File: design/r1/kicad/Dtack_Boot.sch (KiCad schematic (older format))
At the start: 7 parts, among them IC5 ATF16V8QL-15PU, IC6 74174N

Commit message: Initial cleanup
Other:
- note added: "1"
- note added: "Copyright ©2019-2020 Ross Bamford and Contributors.\nOpen Source Hardware licenced under CERN Open Hardware Licence. \nSee https://github.com/roscopeco/rosco_m68k/blob/master/LICENCE.hardware.txt\nOSHWA UK000006 (https://certification.oshwa.org/uk000006.html)\n"
- note added: "DTACK & BOOT"
- note removed: "DTACK\n& BOOT"
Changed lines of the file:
@@
 	6600 2000 6700 1900
-$Comp
-L rosco_m68k-eagle-import:A3L-LOC #FRAME3
-U 1 1 578F4FA5
-P 250 9450
-AR Path="/578F4FA5" Ref="#FRAME3"  Part="1"
-AR Path="/5E53B810/578F4FA5" Ref="#FRAME3"  Part="1"
-F 0 "#FRAME3" H 250 9450 50  0001 C CNN
-F 1 "BOOT line generator" H 250 9450 50  0001 C CNN
-F 2 "" H 250 9450 50  0001 C CNN
-F 3 "" H 250 9450 50  0001 C CNN
-	1    250  9450
-	1    0    0    -1
-$EndComp
 $Comp
 L rosco_m68k-eagle-import:74174N IC6
@@
 Text Notes 5500 7700 0    59   ~ 0
 /BOOT LINE GENERATOR
-Text Notes 13000 10200 0    170  ~ 0
-DTACK\n& BOOT
 NoConn ~ 5300 2900
 NoConn ~ 6200 6200
 NoConn ~ 6200 6500
 NoConn ~ 5300 2200
+Text Notes 12300 10000 0    59   ~ 0
+Copyright ©2019-2020 Ross Bamford and Contributors.\nOpen Source Hardware licenced under CERN Open Hardware Licence. \nSee https://github.com/roscopeco/rosco_m68k/blob/master/LICENCE.hardware.txt\nOSHWA UK000006 (https://certification.oshwa.org/uk000006.html)\n
+Text Notes 12650 10550 0    59   ~ 0
+DTACK & BOOT
+Text Notes 15900 10700 0    59   ~ 0
+1
 Wire Bus Line
 	6700 800  6700 2600

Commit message: Cleanup first pass
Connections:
- net labels added: BOOT, IACK, IODTACK, MFPDS, RAMOE, RW
- net labels removed: /BOOT, /IACK, /IODTACK, /MFPDS, /RAMOE, CONTROL:AS,BERR,BG,BGACK,BR,CLK,DTACK,EVENRAMSEL,EVENROMSEL,EXPSEL,FC0,FC1,FC2,IOSEL,IPL0,IPL1,IPL2,LDS,ODDRAMSEL,ODDROMSEL,RESET,R/W,UDS, R/W
- wire segments 77 -> 65
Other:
- moved on the sheet: IC6A

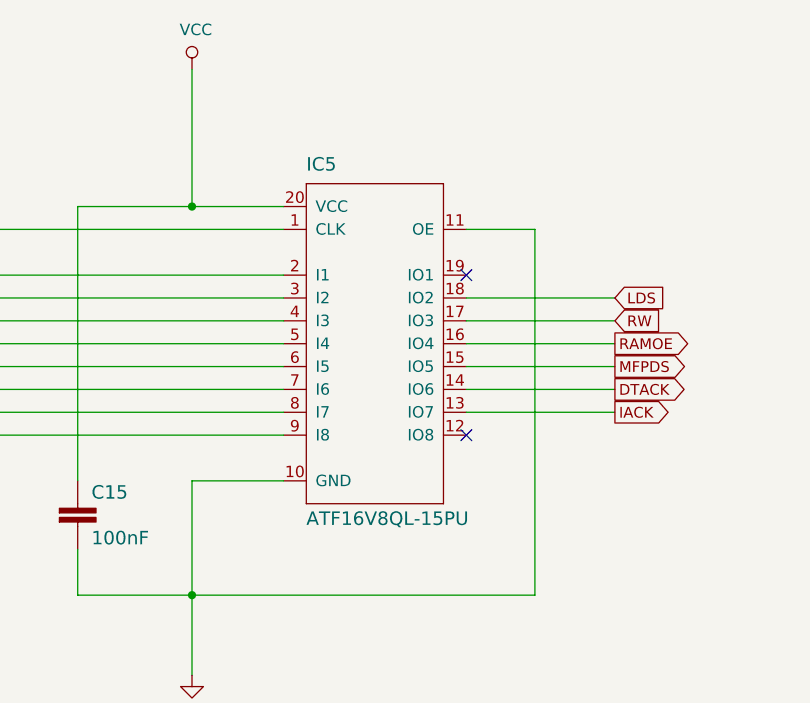
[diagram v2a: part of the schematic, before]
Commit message: Fixing migrated symbols
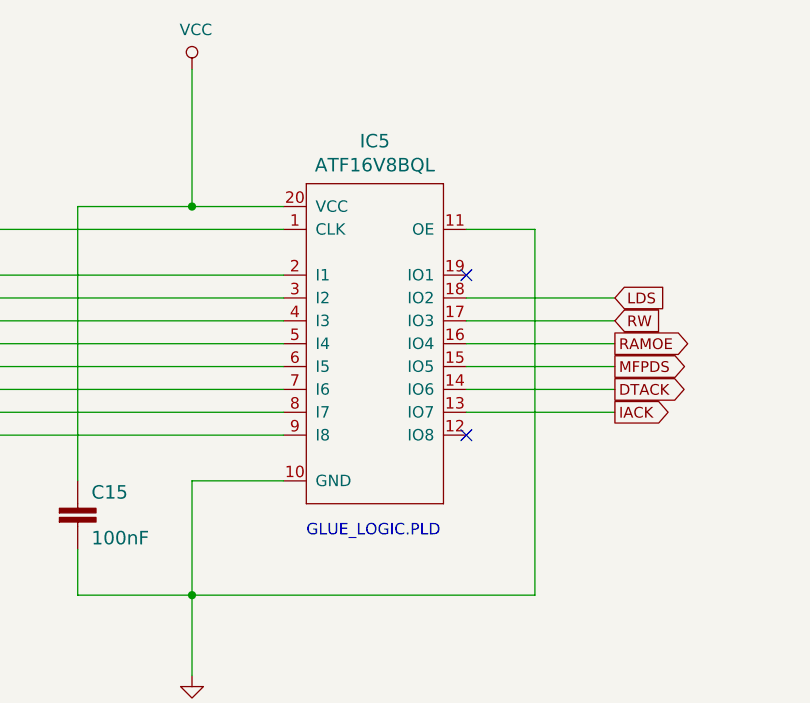
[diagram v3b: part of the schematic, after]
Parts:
- IC5: value ATF16V8QL-15PU -> ATF16V8BQL; footprint rosco_m68k:DIL20 -> (none); MPN ATF16V8QL-15PU -> (none); PROG GLUE_LOGIC.PLD -> (none)
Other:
- note added: "GLUE_LOGIC.PLD"
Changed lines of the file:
@@
-$EndComp
-$Comp
-L rosco_m68k-eagle-import:ATF16V8BP3 IC5
-U 1 1 608347BB
-P 4900 2500
-AR Path="/608347BB" Ref="IC5"  Part="1"
-AR Path="/5E53B810/608347BB" Ref="IC5"  Part="1"
-F 0 "IC5" H 4600 3250 59  0000 L BNN
-F 1 "ATF16V8QL-15PU" H 4600 1700 59  0000 L BNN
-F 2 "rosco_m68k:DIL20" H 4900 2500 50  0001 C CNN
-F 3 "" H 4900 2500 50  0001 C CNN
-F 4 "ATF16V8QL-15PU" H 4900 2500 59  0001 L BNN "MPN"
-F 5 "GLUE_LOGIC.PLD" H 4600 1600 59  0001 L BNN "PROG"
-	1    4900 2500
-	1    0    0    -1
 $EndComp
 $Comp
@@
 Wire Wire Line
 	13200 3150 13200 4200
+$Comp
+L rosco_m68k-eagle-import:ATF16V8BP3 IC5
+U 1 1 5FE89F94
+P 4900 2500
+F 0 "IC5" H 4900 3386 59  0000 C CNN
+F 1 "ATF16V8BQL" H 4900 3281 59  0000 C CNN
+F 2 "" H 4900 2500 50  0001 C CNN
+F 3 "" H 4900 2500 50  0001 C CNN
+	1    4900 2500
+	1    0    0    -1
+$EndComp
+Text Notes 4600 3350 0    50   ~ 0
+GLUE_LOGIC.PLD
 $EndSCHEMATC

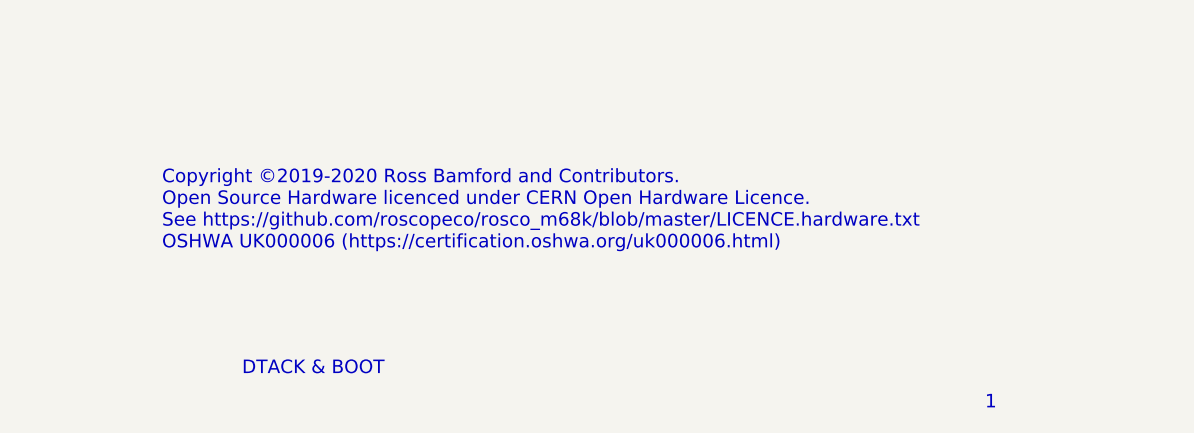
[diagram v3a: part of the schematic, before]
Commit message: Fix #18 and apply suggestions from #17
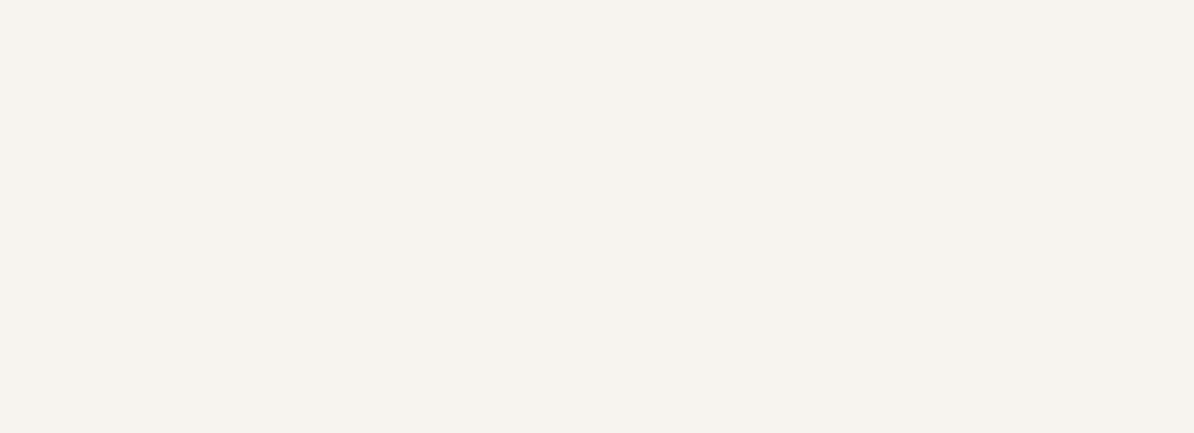
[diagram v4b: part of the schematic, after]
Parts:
- IC5: footprint (none) -> rosco_m68k:DIL20
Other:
- note removed: "1"
- note removed: "Copyright ©2019-2020 Ross Bamford and Contributors.\nOpen Source Hardware licenced under CERN Open Hardware Licence. \nSee https://github.com/roscopeco/rosco_m68k/blob/master/LICENCE.hardware.txt\nOSHWA UK000006 (https://certification.oshwa.org/uk000006.html)\n"
- note removed: "DTACK & BOOT"
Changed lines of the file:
@@
 encoding utf-8
 Sheet 4 6
-Title ""
+Title "DTACK & BOOT"
 Date "2020-02-25"
-Rev ""
+Rev "1"
 Comp ""
-Comment1 ""
-Comment2 ""
-Comment3 ""
-Comment4 ""
+Comment1 "OSHWA UK000006 (https://certification.oshwa.org/uk000006.html)"
+Comment2 "See https://github.com/roscopeco/rosco_m68k/blob/master/LICENCE.hardware.txt"
+Comment3 "Open Source Hardware licenced under CERN Open Hardware Licence"
+Comment4 "Copyright 2019-2020 Ross Bamford and Contributors"
 $EndDescr
 Wire Wire Line
@@
 NoConn ~ 5200 7750
 NoConn ~ 5300 2200
-Text Notes 12300 10000 0    59   ~ 0
-Copyright ©2019-2020 Ross Bamford and Contributors.\nOpen Source Hardware licenced under CERN Open Hardware Licence. \nSee https://github.com/roscopeco/rosco_m68k/blob/master/LICENCE.hardware.txt\nOSHWA UK000006 (https://certification.oshwa.org/uk000006.html)\n
-Text Notes 12650 10550 0    59   ~ 0
-DTACK & BOOT
-Text Notes 15900 10700 0    59   ~ 0
-1
 $Comp
 L power:GND #PWR0125
@@
 F 0 "IC5" H 4900 3386 59  0000 C CNN
 F 1 "ATF16V8BQL" H 4900 3281 59  0000 C CNN
-F 2 "" H 4900 2500 50  0001 C CNN
+F 2 "rosco_m68k:DIL20" H 4900 2500 50  0001 C CNN
 F 3 "" H 4900 2500 50  0001 C CNN
 	1    4900 2500
